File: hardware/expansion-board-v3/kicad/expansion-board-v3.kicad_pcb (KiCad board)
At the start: 6 copper layers, 100 x 62 mm, 157 parts, among them J1 PinHeader_2x20_P2.54mm_Vertic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, J2 U.FL_Hirose_U.FL-R-SMT-1_Vert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, J4 USB_C_Receptacle_HRO_TYPE-C-3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, J5 U.FL_Hirose_U.FL-R-SMT-1_Vert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, J6 U.FL_Hirose_U.FL-R-SMT-1_Vert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, J7 U.FL_Hirose_U.FL-R-SMT-1_Vert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, J8 U.FL_Hirose_U.FL-R-SMT-1_Vert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, Q2 SOT-23, Q3 SOT-23, Q4 SOT-23, Q5 SOT-23, SW1 SolderJumper-2_P1.3mm_Open_Pa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, SW2 SolderJumper-2_P1.3mm_Open_Pa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, U1 SOT-23-5, U10 QFN-48-1EP_7x7mm_P0.5mm_EP5.1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, U11 DFN-8-1EP_2x2mm_P0.5mm_EP0.86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, U12 SOT-363_SC-70-6, U13 AD8319_LFCSP-8-EP, U14 MSOP-8_3x3mm_P0.65mm, U15 SOT-23-6, U16 SOT-363_SC-70-6, U17 SOT-363_SC-70-6, U2 SOT-23-5, U3 SOT-23-5, U4 BNO085_LGA-28, U5 BMP388_LGA-10, U6 LGA-16_3x3mm_P0.5mm, U7 ATGM336H_LCC-18, U8 QFN-56-1EP_7x7mm_P0.4mm_EP3.2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, U9 SOIC-8_5.3x5.3mm_P1.27mm, Y1 Crystal_SMD_3225-4Pin_3.2x2.5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, Y2 Crystal_SMD_3225-4Pin_3.2x2.5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, Y3 Crystal_SMD_3215-2Pin_3.2x1.5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

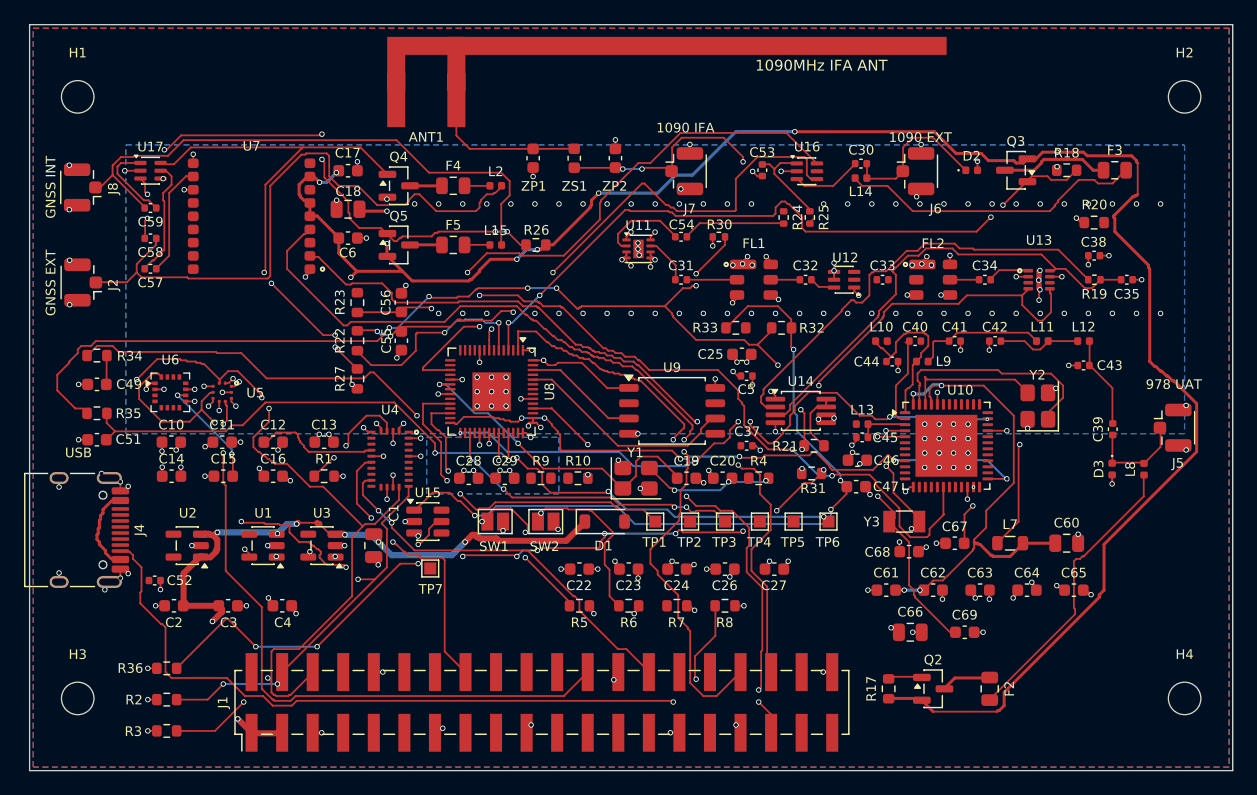
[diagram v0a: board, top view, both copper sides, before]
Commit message: fix(v3): 收敛 GNSS 路由并冻结 1090MHz IFA
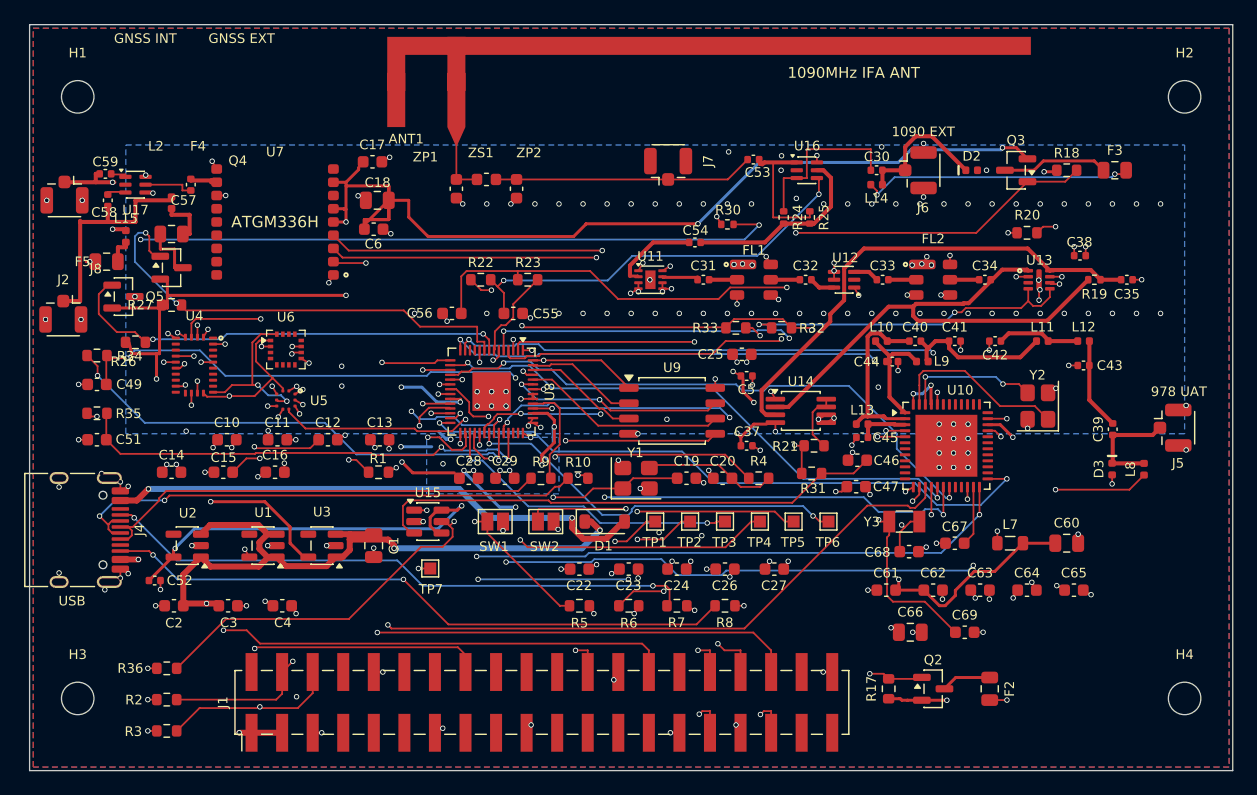
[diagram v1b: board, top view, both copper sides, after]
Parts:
- moved R26 34.2 mm to (58.8, 76.4), turned to 0 degrees
- moved L15 30.8 mm to (58.0, 67.6), turned to 90 degrees
- moved F5 28.8 mm to (56.4, 69.7)
- moved L2 27.0 mm to (61.8, 64.8), turned to 90 degrees
- moved F4 23.8 mm to (61.8, 67.4)
- moved Q5 23.3 mm to (57.8, 72.6)
- moved Q4 20.1 mm to (61.8, 70.2)
- moved U4 18.0 mm to (63.7, 78.3)
- moved R27 16.6 mm to (61.8, 73.3), turned to 0 degrees
- moved R23 14.3 mm to (91.4, 71.2), turned to 180 degrees
- moved R22 11.4 mm to (87.5, 71.2), turned to 0 degrees
- moved U6 10.2 mm to (71.3, 77.0)
- moved C55 9.57 mm to (90.2, 74.0), turned to 0 degrees
- moved ZP2 8.60 mm to (90.5, 63.6), turned to -90 degrees
- moved C57 7.75 mm to (63.4, 63.3), turned to -90 degrees
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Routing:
- net SUBG_MISO: track 0.00 -> 78.2 mm, vias 0 -> 2
- net LEVEL_BIAS: track 2.45 -> 72.1 mm, vias 0 -> 5
- net SUBG_TMSC: track 0.00 -> 63.7 mm, vias 0 -> 3
- net GNSS_RXD: track 0.00 -> 61.1 mm, vias 0 -> 2
- net 3V3_RF: track 6.47 -> 66.8 mm, vias 8 -> 16
- net BIAS_EN_978: track 2.97 -> 60.9 mm, vias 0 -> 3
- net SUBG_SCK: track 0.00 -> 57.5 mm, vias 0 -> 3
- net SUBG_MOSI: track 0.00 -> 51.1 mm, vias 0 -> 3
- net USB_CC1: track 0.00 -> 49.7 mm, vias 0 -> 2
- net SUBG_SYNC: track 0.00 -> 48.6 mm, vias 0 -> 2
- net SUBG_CSN: track 0.00 -> 46.3 mm, vias 0 -> 2
- net USB_VBUS: track 7.33 -> 52.8 mm, vias 0 -> 3
- net USB_DM: track 0.00 -> 43.9 mm, vias 0 -> 2
- net ADSB_RXD: track 0.00 -> 41.2 mm, vias 0 -> 2
- net RP_1V1: track 1.61 -> 42.6 mm, vias 2 -> 10
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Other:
- board text added: "3V3-D"
- board text added: "3V3-G"
- board text added: "3V3-RF"
- board text added: "AD8313"
- board text added: "AD8319"
- board text added: "ATGM336H"
- board text added: "BMP388"
- board text added: "BNO085"
- board text added: "CC1312R"
- board text added: "LNA1"
- board text added: "LNA2"
- board text added: "QMC5883"
- board text added: "RP2040"
- board text added: "SW1090"
- board text added: "SWGNSS"
- board text added: "TLV3501"
- board text added: "V3.2 2026-08"
- board text added: "W25Q128"
- board text removed: "1090 IFA"
- board text removed: "V3.5 2026-08"

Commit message: fix(v3): 固化人工布局并收紧重建验收
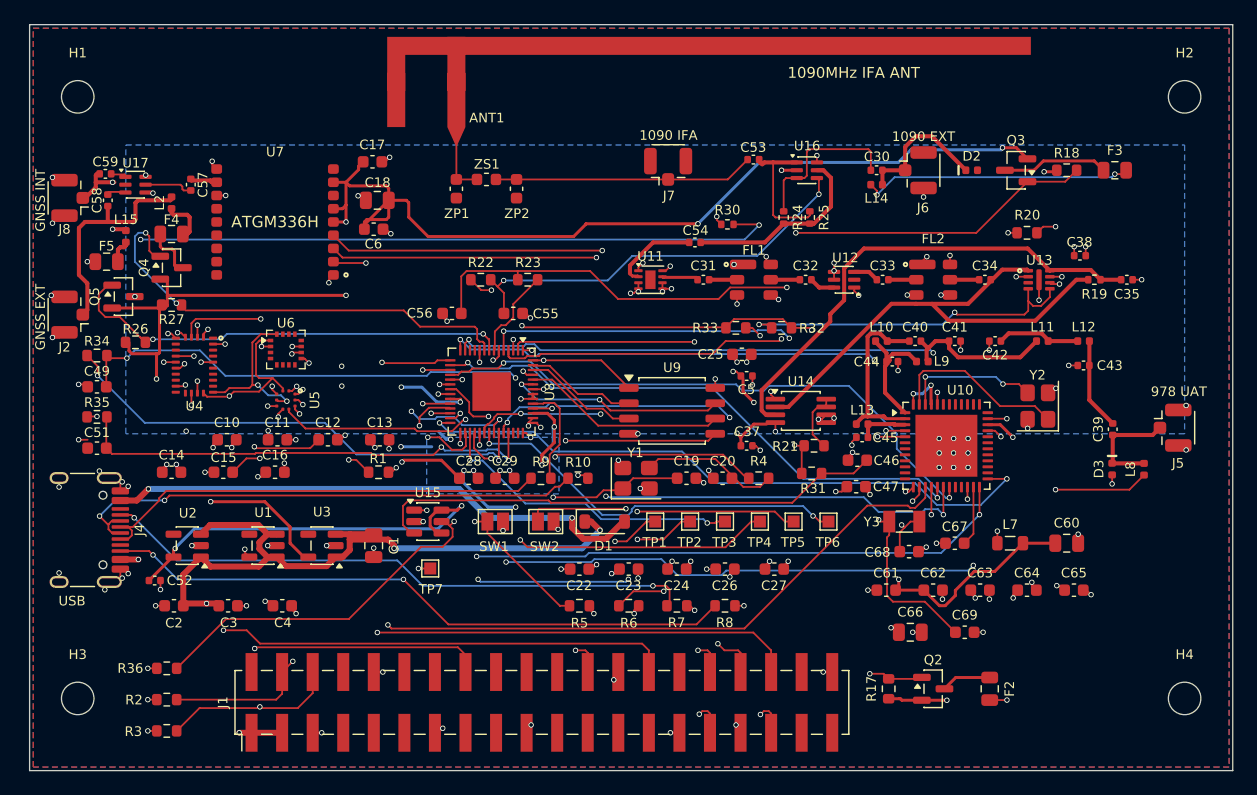
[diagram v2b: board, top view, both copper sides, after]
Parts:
- moved C51 0.70 mm to (55.6, 85.2)
- moved J2 0.41 mm to (52.9, 74.1), turned to 180 degrees
- moved R35 0.30 mm to (55.6, 82.6)
- moved C49 0.20 mm to (55.6, 80.1)
- moved J8 0.20 mm to (52.9, 64.4), turned to 180 degrees
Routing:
- net 3V3_GNSS: track 206.7 -> 195.5 mm
- net GND: track 90.5 -> 97.3 mm, vias 217 -> 132
- net DET_IN: track 42.8 -> 40.9 mm
- net SW1_J3: track 13.1 -> 11.5 mm
- net RP_1V1: track 42.6 -> 44.1 mm
- net 3V3_DIG: track 37.7 -> 38.9 mm
- net ANT_SEL_GNSS_A: track 48.9 -> 50.1 mm
- net ANT_GNSS_INT: track 10.3 -> 9.57 mm
- net I2C_SCL: track 54.1 -> 54.8 mm
- net RF_DET_OUT: track 122.3 -> 122.9 mm
- net ANT_SEL_GNSS_B: track 42.1 -> 42.6 mm
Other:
- board text added: "1090 IFA"
- board text added: "V3.6 2026-08"
- board text removed: "V3.2 2026-08"

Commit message: fix(v3): reroute GNSS antenna bias control
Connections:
- Q4 pad 1: ANT_SEL_GNSS_B -> ANT_SEL_GNSS_A
- Q5 pad 1: ANT_SEL_GNSS_A -> ANT_SEL_GNSS_B
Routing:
- net ANT_SEL_GNSS_A: track 50.1 -> 43.6 mm, vias 3 -> 4
- net ANT_SEL_GNSS_B: track 42.6 -> 48.5 mm, vias 3 -> 4
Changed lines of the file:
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@@
 			(layers "F.Cu" "F.Mask" "F.Paste")
 			(roundrect_rratio 0.25)
-			(net "ANT_SEL_GNSS_B")
+			(net "ANT_SEL_GNSS_A")
 		)
 		(pad "2" smd roundrect
@@
 			(layers "F.Cu" "F.Mask" "F.Paste")
 			(roundrect_rratio 0.25)
-			(net "ANT_SEL_GNSS_A")
+			(net "ANT_SEL_GNSS_B")
 		)
 		(pad "2" smd roundrect
@@
 	)
 	(segment
-		(start 60.4 69.25)
-		(end 60.8625 69.25)
-		(width 0.15)
-		(layer "F.Cu")
-		(net "ANT_SEL_GNSS_B")
-	)
-	(segment
-		(start 59.95 67.6)
-		(end 59.95 68.8)
-		(width 0.15)
-		(layer "F.Cu")
-		(net "ANT_SEL_GNSS_B")
-	)
-	(segment
 		(start 87.8 76.4833)
 		(end 87.8 77.0625)
@@
 	)
 	(segment
-		(start 59.95 68.8)
-		(end 60.4 69.25)
-		(width 0.15)
-		(layer "F.Cu")
-		(net "ANT_SEL_GNSS_B")
-	)
-	(segment
 		(start 87.2 76.15)
 		(end 87.4 76.35)
@@
 	)
 	(segment
-		(start 59.65 67.3)
-		(end 59.95 67.6)
-		(width 0.15)
-		(layer "F.Cu")
-		(net "ANT_SEL_GNSS_B")
-	)
-	(segment
 		(start 62.2 73.15)
 		(end 62.225 73.15)
@@
 	)
 	(segment
-		(start 55.75 73.75)
-		(end 56.3 74.3)
-		(width 0.15)
-		(layer "F.Cu")
-		(net "ANT_SEL_GNSS_A")
-	)
-	(segment
 		(start 59.225 76)
 		(end 59.625 76.4)
@@
 	)
 	(segment
-		(start 56.3 74.3)
-		(end 57.5 74.3)
-		(width 0.15)
-		(layer "F.Cu")
-		(net "ANT_SEL_GNSS_A")
-	)
-	(segment
 		(start 60.2333 63.95)
 		(end 60.25 63.9667)
@@
 	)
 	(segment
-		(start 55.75 72.4)
-		(end 55.75 73.75)
-		(width 0.15)
-		(layer "F.Cu")
-		(net "ANT_SEL_GNSS_A")
-	)
-	(segment
 		(start 59.95 76.15)
 		(end 60.25 76.15)
@@
 	)
 	(segment
-		(start 57.5 74.3)
-		(end 59.2 76)
-		(width 0.15)
-		(layer "F.Cu")
-		(net "ANT_SEL_GNSS_A")
-	)
-	(segment
-		(start 56.5 71.65)
-		(end 56.8625 71.65)
-		(width 0.15)
-		(layer "F.Cu")
-		(net "ANT_SEL_GNSS_A")
-	)
-	(segment
 		(start 88.15 76.15)
 		(end 88.175 76.15)
@@
 		(net "ANT_SEL_GNSS_A")
 	)
-	(segment
-		(start 55.75 72.4)
-		(end 56.5 71.65)
-		(width 0.15)
-		(layer "F.Cu")
-		(net "ANT_SEL_GNSS_A")
-	)
 	(via
 		(at 87.7 75.7)
@@
 	)
 	(segment
-		(start 60.25 64)
-		(end 60.25 76.15)
-		(width 0.15)
-		(layer "In2.Cu")
-		(net "ANT_SEL_GNSS_A")
-	)
-	(segment
 		(start 59.64 63.3)
 		(end 62.54 63.3)
@@
 		(net "TL_PWM")
 	)
+	(segment
+		(start 60.8625 69.25)
+		(end 60.4 69.25)
+		(width 0.15)
+		(layer "F.Cu")
+		(net "ANT_SEL_GNSS_A")
+	)
+	(via
+		(at 60.4 69.25)
+		(size 0.5)
+		(drill 0.3)
+		(layers "F.Cu" "B.Cu")
+		(net "ANT_SEL_GNSS_A")
+	)
+	(via
+		(at 57.7 70.8125)
+		(size 0.5)
+		(drill 0.3)
+		(layers "F.Cu" "B.Cu")
+		(net "ANT_SEL_GNSS_B")
+	)
+	(segment
+		(start 57.7 70.8125)
+		(end 56.8625 71.65)
+		(width 0.15)
+		(layer "F.Cu")
+		(net "ANT_SEL_GNSS_B")
+	)
+	(segment
+		(start 60.25 64.0)
+		(end 60.25 69.1)
+		(width 0.15)
+		(layer "In2.Cu")
+		(net "ANT_SEL_GNSS_A")
+	)
+	(segment
+		(start 60.25 69.1)
+		(end 60.25 76.15)
+		(width 0.15)
+		(layer "In2.Cu")
+		(net "ANT_SEL_GNSS_A")
+	)
+	(segment
+		(start 60.4 69.25)
+		(end 60.25 69.1)
+		(width 0.15)
+		(layer "In2.Cu")
+		(net "ANT_SEL_GNSS_A")
+	)
+	(segment
+		(start 57.7 70.8125)
+		(end 57.7 69.5)
+		(width 0.15)
+		(layer "In2.Cu")
+		(net "ANT_SEL_GNSS_B")
+	)
+	(segment
+		(start 57.7 69.5)
+		(end 57.4 69.2)
+		(width 0.15)
+		(layer "In2.Cu")
+		(net "ANT_SEL_GNSS_B")
+	)
+	(segment
+		(start 57.4 69.2)
+		(end 57.4 66.5)
+		(width 0.15)
+		(layer "In2.Cu")
+		(net "ANT_SEL_GNSS_B")
+	)
+	(segment
+		(start 57.4 66.5)
+		(end 57.9 66.0)
+		(width 0.15)
+		(layer "In2.Cu")
+		(net "ANT_SEL_GNSS_B")
+	)
+	(segment
+		(start 57.9 66.0)
+		(end 58.35 66.0)
+		(width 0.15)
+		(layer "In2.Cu")
+		(net "ANT_SEL_GNSS_B")
+	)
+	(segment
+		(start 58.35 66.0)
+		(end 59.65 67.3)
+		(width 0.15)
+		(layer "In2.Cu")
+		(net "ANT_SEL_GNSS_B")
+	)
 	(zone

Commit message: fix(v3): bump GNSS ECO board revision to V3.7
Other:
- board text added: "V3.7 2026-08"
- board text removed: "V3.6 2026-08"
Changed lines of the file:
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@@
 		)
 	)
-	(gr_text "V3.6   2026-08"
+	(gr_text "V3.7   2026-08"
 		(at 100 80 0)
 		(layer "B.SilkS")
